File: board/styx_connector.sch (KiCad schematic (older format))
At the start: 2 parts, among them J4 Styx_P4, J5 Styx_P5

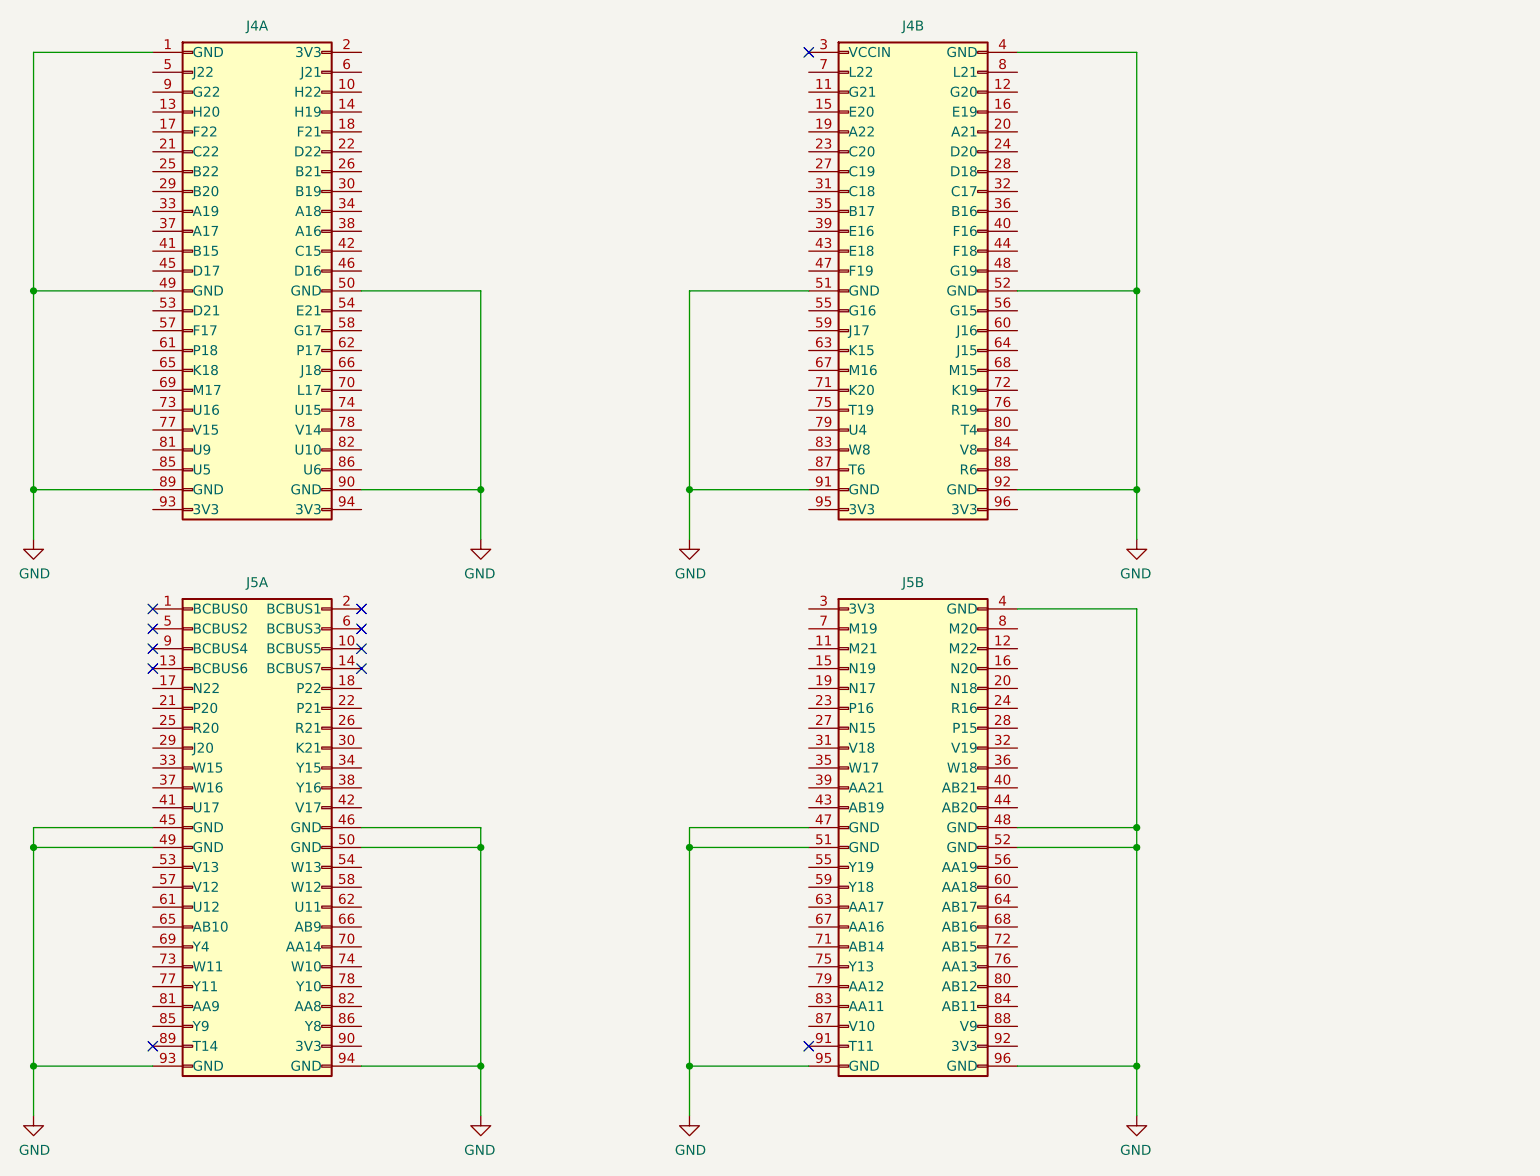
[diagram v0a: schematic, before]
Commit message: Board: 5/8 of the data lanes routed
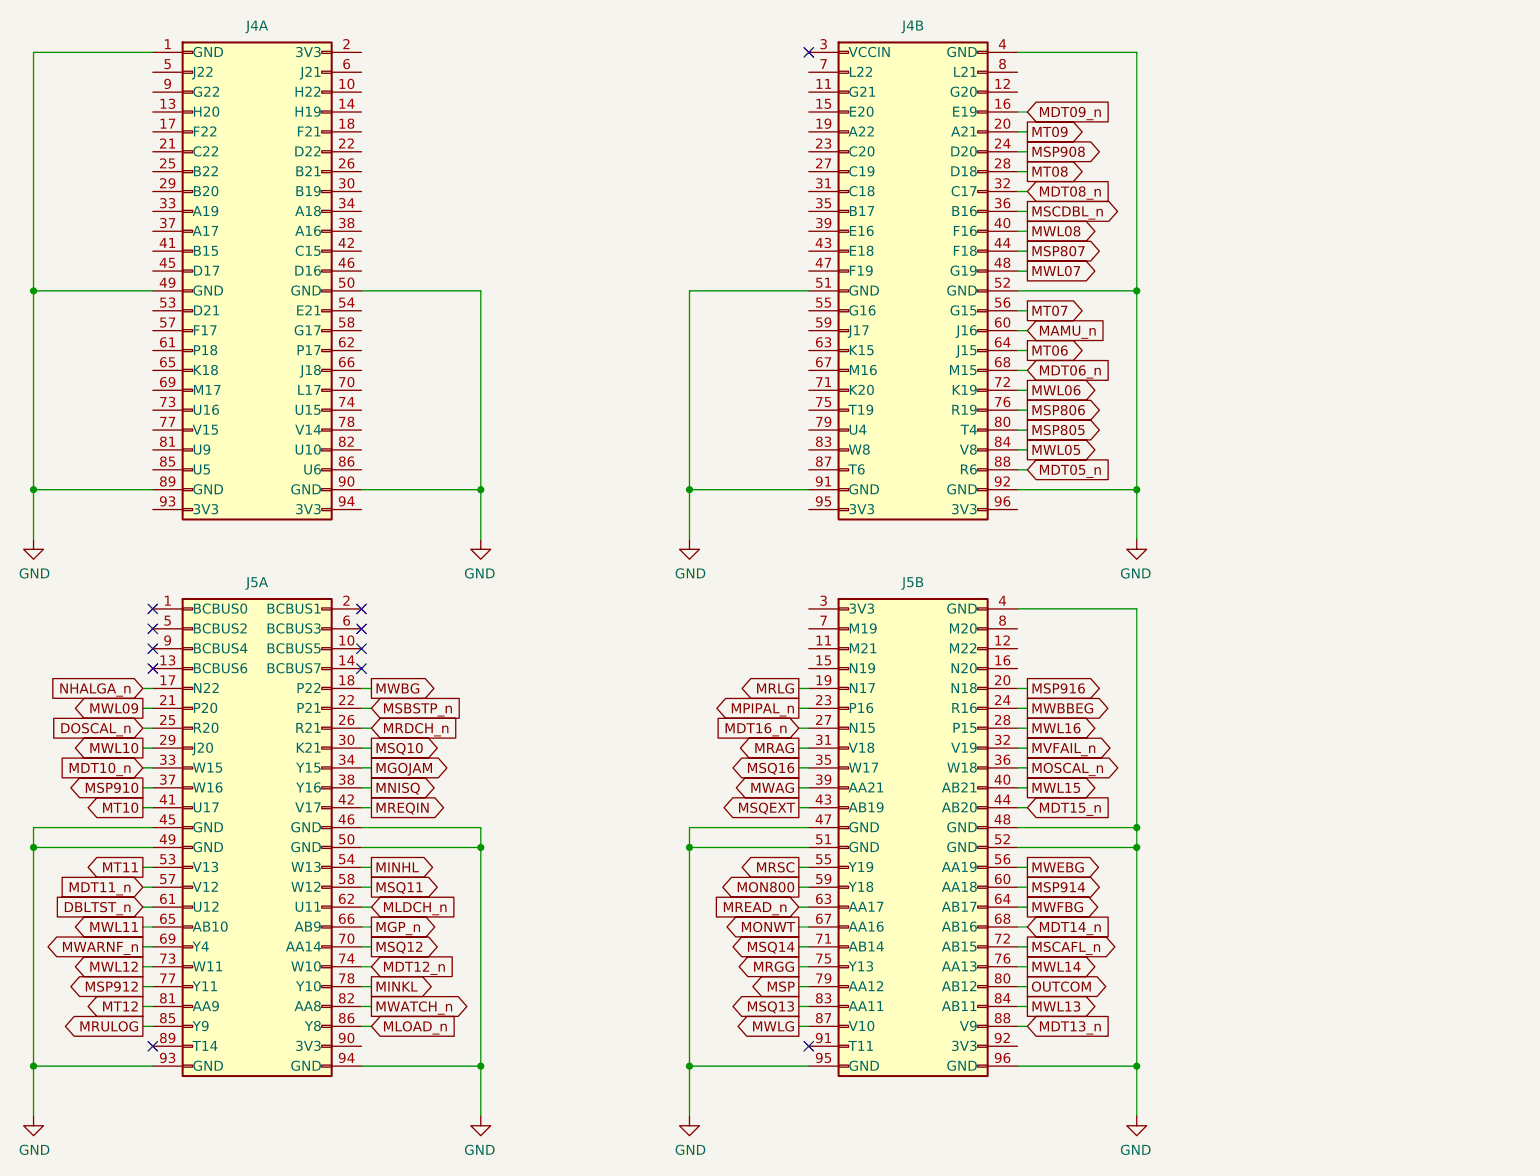
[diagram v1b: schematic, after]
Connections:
- net MDT09_n: now reaches J4.16 (E19)
- net MT09: now reaches J4.20 (A21)
- net MSP908: now reaches J4.24 (D20)
- net MT08: now reaches J4.28 (D18)
- net MDT08_n: now reaches J4.32 (C17)
- net MSCDBL_n: now reaches J4.36 (B16)
- net MWL08: now reaches J4.40 (F16)
- net MSP807: now reaches J4.44 (F18)
- net MWL07: now reaches J4.48 (G19)
- net MT07: now reaches J4.56 (G15)
- net MAMU_n: now reaches J4.60 (J16)
- net MT06: now reaches J4.64 (J15)
- net MDT06_n: now reaches J4.68 (M15)
- net MWL06: now reaches J4.72 (K19)
- net MSP806: now reaches J4.76 (R19)
- net MSP805: now reaches J4.80 (T4)
- net MWL05: now reaches J4.84 (V8)
- net MDT05_n: now reaches J4.88 (R6)
- net NHALGA_n: now reaches J5.17 (N22)
- net MWBG: now reaches J5.18 (P22)
- net MWL09: now reaches J5.21 (P20)
- net MSBSTP_n: now reaches J5.22 (P21)
- net DOSCAL_n: now reaches J5.25 (R20)
- net MRDCH_n: now reaches J5.26 (R21)
- net MWL10: now reaches J5.29 (J20)
- net MSQ10: now reaches J5.30 (K21)
- net MDT10_n: now reaches J5.33 (W15)
- net MGOJAM: now reaches J5.34 (Y15)
- net MSP910: now reaches J5.37 (W16)
- net MNISQ: now reaches J5.38 (Y16)
- net MT10: now reaches J5.41 (U17)
- net MREQIN: now reaches J5.42 (V17)
- net MT11: now reaches J5.53 (V13)
- net MINHL: now reaches J5.54 (W13)
- net MDT11_n: now reaches J5.57 (V12)
- net MSQ11: now reaches J5.58 (W12)
- net DBLTST_n: now reaches J5.61 (U12)
- net MLDCH_n: now reaches J5.62 (U11)
- net MWL11: now reaches J5.65 (AB10)
- net MGP_n: now reaches J5.66 (AB9)
- net MWARNF_n: now reaches J5.69 (Y4)
- net MSQ12: now reaches J5.70 (AA14)
- net MWL12: now reaches J5.73 (W11)
- net MDT12_n: now reaches J5.74 (W10)
- net MSP912: now reaches J5.77 (Y11)
- net MINKL: now reaches J5.78 (Y10)
- net MT12: now reaches J5.81 (AA9)
- net MWATCH_n: now reaches J5.82 (AA8)
- net MRULOG: now reaches J5.85 (Y9)
- net MLOAD_n: now reaches J5.86 (Y8)
- net MRLG: now reaches J5.19 (N17)
- net MSP916: now reaches J5.20 (N18)
- net MPIPAL_n: now reaches J5.23 (P16)
- net MWBBEG: now reaches J5.24 (R16)
- net MDT16_n: now reaches J5.27 (N15)
- net MWL16: now reaches J5.28 (P15)
- net MRAG: now reaches J5.31 (V18)
- net MVFAIL_n: now reaches J5.32 (V19)
- net MSQ16: now reaches J5.35 (W17)
- net MOSCAL_n: now reaches J5.36 (W18)
- net MWAG: now reaches J5.39 (AA21)
- net MWL15: now reaches J5.40 (AB21)
- net MSQEXT: now reaches J5.43 (AB19)
- net MDT15_n: now reaches J5.44 (AB20)
- net MRSC: now reaches J5.55 (Y19)
- net MWEBG: now reaches J5.56 (AA19)
- net MON800: now reaches J5.59 (Y18)
- net MSP914: now reaches J5.60 (AA18)
- net MREAD_n: now reaches J5.63 (AA17)
- net MWFBG: now reaches J5.64 (AB17)
- net MONWT: now reaches J5.67 (AA16)
- net MDT14_n: now reaches J5.68 (AB16)
- net MSQ14: now reaches J5.71 (AB14)
- net MSCAFL_n: now reaches J5.72 (AB15)
- net MRGG: now reaches J5.75 (Y13)
- net MWL14: now reaches J5.76 (AA13)
- net MSP: now reaches J5.79 (AA12)
- net OUTCOM: now reaches J5.80 (AB12)
- net MSQ13: now reaches J5.83 (AA11)
- net MWL13: now reaches J5.84 (AB11)
- net MWLG: now reaches J5.87 (V10)
- net MDT13_n: now reaches J5.88 (V9)

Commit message: Board: Finished routing AGC signals; still need to route 3v3 and ground to RTL circuits
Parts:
- added J6: Conn_02x12_Odd_Even, Connector_PinSocket_2.54mm:PinSocket_2x12_P2.54mm_Vertical, symbol Connector_Generic:Conn_02x12_Odd_Even
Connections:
- net GND: now also J6.23 (Pin_23), J6.24 (Pin_24)
- net DBG7: now reaches J4.10 (H22)
- net DBG7: now also J6.15 (Pin_15)
- net DBG3: now reaches J4.13 (H20)
- net DBG3: now also J6.7 (Pin_7)
- net DBG8: now reaches J4.14 (H19)
- net DBG8: now also J6.17 (Pin_17)
- net DBG4: now reaches J4.17 (F22)
- net DBG4: now also J6.9 (Pin_9)
- net DBG9: now reaches J4.18 (F21)
- net DBG9: now also J6.19 (Pin_19)
- net DBG_3V3: now reaches J4.2 (3V3)
- net DBG_3V3: now also J6.1 (Pin_1), J6.2 (Pin_2)
- net DBG5: now reaches J4.21 (C22)
- net DBG5: now also J6.11 (Pin_11)
- net DBG10: now reaches J4.22 (D22)
- net DBG10: now also J6.21 (Pin_21)
- net MT01: now reaches J4.25 (B22)
- net MBR1: now reaches J4.26 (B21)
- net MDT01_n: now reaches J4.29 (B20)
- net MST1: now reaches J4.30 (B19)
- net MWL01: now reaches J4.33 (A19)
- net STRT1: now reaches J4.34 (A18)
- net MWL02: now reaches J4.37 (A17)
- net STRT2: now reaches J4.38 (A16)
- net MDT02_n: now reaches J4.41 (B15)
- net MST2: now reaches J4.42 (C15)
- net MT02: now reaches J4.45 (D17)
- net MBR2: now reaches J4.46 (D16)
- net DBG1: now reaches J4.5 (J22)
- net DBG1: now also J6.3 (Pin_3)
- net MSP902: now reaches J4.53 (D21)
- net MIIP: now reaches J4.54 (E21)
- net MT03: now reaches J4.57 (F17)
- net MDT03_n: now reaches J4.58 (G17)
- net DBG6: now reaches J4.6 (J21)
- net DBG6: now also J6.13 (Pin_13)
- net MWL03: now reaches J4.61 (P18)
- net MST3: now reaches J4.62 (P17)
- net MSP803: now reaches J4.65 (K18)
- net MNHSBF_n: now reaches J4.66 (J18)
- net SIGNY: now reaches J4.69 (M17)
- net MNHNC_n: now reaches J4.70 (L17)
- net MWL04: now reaches J4.73 (U16)
- net MTCSA_n: now reaches J4.74 (U15)
- net MT04: now reaches J4.77 (V15)
- net MDT04_n: now reaches J4.78 (V14)
- net MSP904: now reaches J4.81 (U9)
- net MCTRAL_n: now reaches J4.82 (U10)
- net MT05: now reaches J4.85 (U5)
- net MWCH: now reaches J4.86 (U6)
- net DBG2: now reaches J4.9 (G22)
- net DBG2: now also J6.5 (Pin_5)
- net DBG12: now reaches J4.11 (G21)
- net DBG12: now also J6.6 (Pin_6)
- net DBG14: now reaches J4.12 (G20)
- net DBG14: now also J6.10 (Pin_10)
- net MSTPIT_n: now reaches J4.15 (E20)
- net MWG: now reaches J4.19 (A22)
- net MONWBK_n: now reaches J4.23 (C20)
- net MPAL_n: now reaches J4.27 (C19)
- net MWQG: now reaches J4.31 (C18)
- net MSTP_n: now reaches J4.35 (B17)
- net MSTRT_n: now reaches J4.39 (E16)
- net MWYG: now reaches J4.43 (E18)
- net MDT07_n: now reaches J4.47 (F19)
- net ALGA: now reaches J4.55 (G16)
- net MONPAR_n: now reaches J4.59 (J17)
- net MRCH: now reaches J4.63 (K15)
- net MRPTAL_n: now reaches J4.67 (M16)
- net DBG11: now reaches J4.7 (L22)
- net DBG11: now also J6.4 (Pin_4)
- net MWZG: now reaches J4.71 (K20)
- net MTCSAI_n: now reaches J4.75 (T19)
- net MNHRPT_n: now reaches J4.79 (U4)
- net DBG13: now reaches J4.8 (L21)
- net DBG13: now also J6.8 (Pin_8)
- net MWSG: now reaches J4.83 (W8)
- net MTCAL_n: now reaches J4.87 (T6)
- net DBG16: now reaches J5.11 (M21)
- net DBG16: now also J6.14 (Pin_14)
- net DBG19: now reaches J5.12 (M22)
- net DBG19: now also J6.20 (Pin_20)
- net DBG17: now reaches J5.15 (N19)
- net DBG17: now also J6.16 (Pin_16)
- net DBG20: now reaches J5.16 (N20)
- net DBG20: now also J6.22 (Pin_22)
- net DBG15: now reaches J5.7 (M19)
- net DBG15: now also J6.12 (Pin_12)
- net DBG18: now reaches J5.8 (M20)
- net DBG18: now also J6.18 (Pin_18)
- no-connect marks 11 -> 18
